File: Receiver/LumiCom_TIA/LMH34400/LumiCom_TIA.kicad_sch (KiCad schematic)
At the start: 0 parts

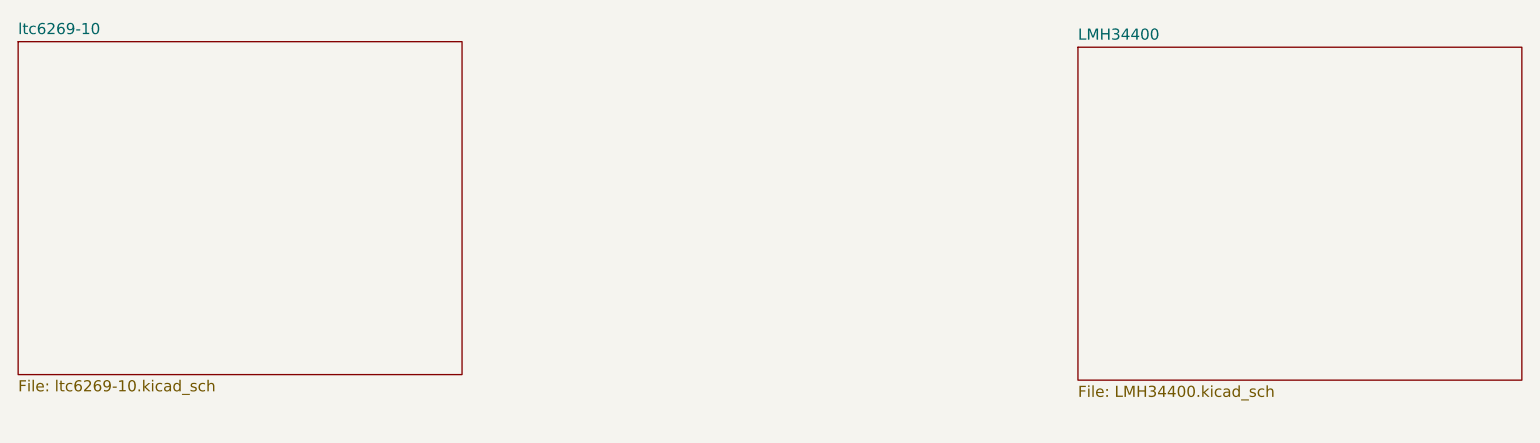
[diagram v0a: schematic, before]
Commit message: Multiple updates
SMA, Screw terminals, track widths, added some optional 0 ohm bypass resistors
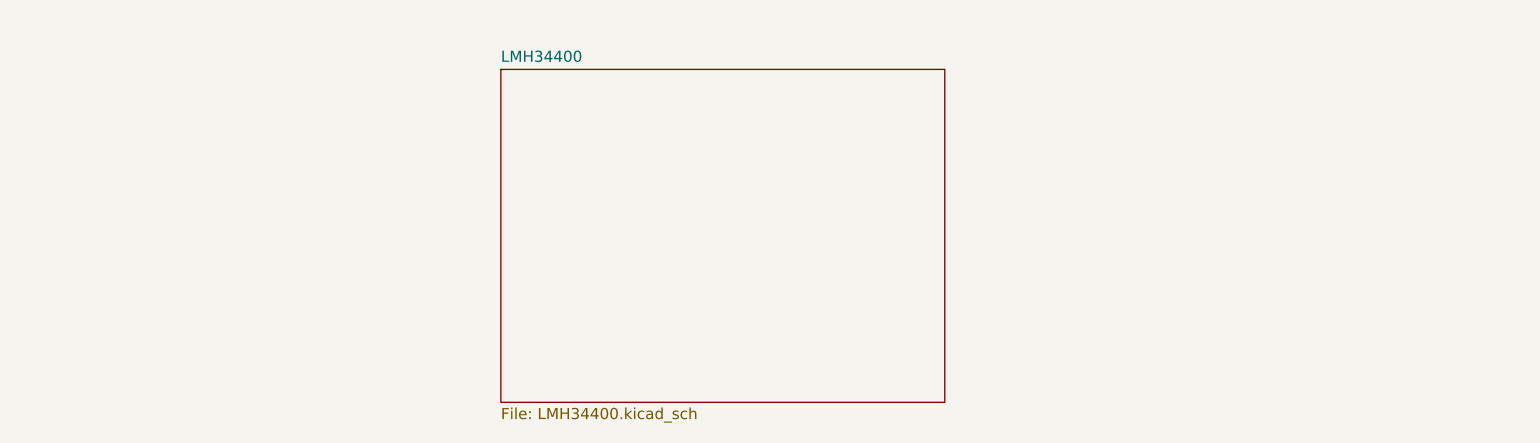
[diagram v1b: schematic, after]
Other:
- removed sheet ltc6269-10
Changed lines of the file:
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@@
 	(paper "A4")
 	(sheet
-		(at 62.865 62.865)
-		(size 50.8 38.1)
-		(fields_autoplaced yes)
-		(stroke
-			(width 0.1524)
-			(type solid)
-		)
-		(fill
-			(color 0 0 0 0.0000)
-		)
-		(property "Sheetname" "ltc6269-10"
-			(at 62.865 62.1534 0)
-			(effects
-				(font
-					(size 1.27 1.27)
-				)
-				(justify left bottom)
-			)
-		)
-		(property "Sheetfile" "ltc6269-10.kicad_sch"
-			(at 62.865 101.5496 0)
-			(effects
-				(font
-					(size 1.27 1.27)
-				)
-				(justify left top)
-			)
-		)
-		(instances
-			(project "LumiCom_TIA"
-				(path "/27381ed8-96e6-4041-ba7f-c08f9d949351"
-					(page "4")
-				)
-			)
-		)
-	)
-	(sheet
-		(at 184.15 63.5)
+		(at 118.11 66.04)
 		(size 50.8 38.1)
 		(fields_autoplaced yes)
@@
 		)
 		(property "Sheetname" "LMH34400"
-			(at 184.15 62.7884 0)
+			(at 118.11 65.3284 0)
 			(effects
 				(font
@@
 		)
 		(property "Sheetfile" "LMH34400.kicad_sch"
-			(at 184.15 102.1846 0)
+			(at 118.11 104.7246 0)
 			(effects
 				(font
